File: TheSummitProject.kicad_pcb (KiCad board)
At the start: 2 copper layers, 120 x 80 mm, 81 parts, among them IC1 STM32U5F7VJT6, J1 Cortex SWD, J10 VSYS, J11 GPS PWR, J12 Sensor PWR, J13 3.3v LORA, J2 USB C, J3 Battery Connector, J4 Screen FPC, J5 Micro_SD_Card_Det1, J6 GPS, J7 LoRa, J8 Sensors, J9 RCC, Q1 NMOS, SW1 SW_SPDT, SW2 PWR_BTN, U1 NPM1300-CAAA-R, U2 USBLC6-2SC6, U3 USBLC6-2SC6, Y1 16Mhz, Y2 32.768Khz

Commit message: modify lora
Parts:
- moved J13 160.8 mm to (125.5, 106.5)
- moved D1 0.50 mm to (129.0, 104.0)
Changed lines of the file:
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@@
 	(footprint "Connector_PinHeader_2.54mm:PinHeader_1x02_P2.54mm_Vertical"
 		(layer "F.Cu")
-		(at 266.795 29.795)
+		(at 125.5 106.46)
 		(descr "Through hole straight pin header, 1x02, 2.54mm pitch, single row")
 		(tags "Through hole pin header THT 1x02 2.54mm single row")
@@
 	(footprint "LED_SMD:LED_RGB_1210"
 		(layer "F.Cu")
-		(at 128.5 104 -90)
+		(at 129 104 -90)
 		(descr "RGB LED 3.2x2.7mm http://www.avagotech.com/docs/AV02-0610EN")
 		(tags "LED 3227")

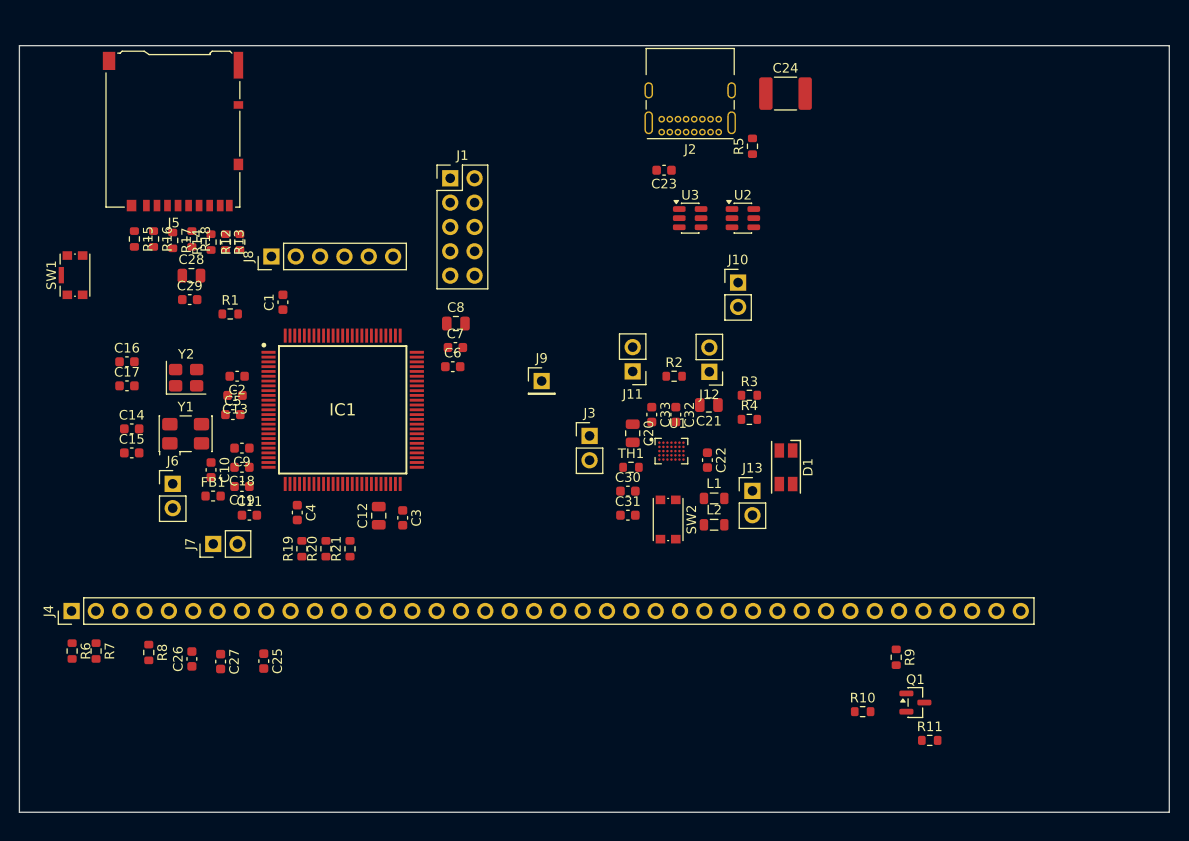
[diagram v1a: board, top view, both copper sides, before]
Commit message: wire usbc and cystal
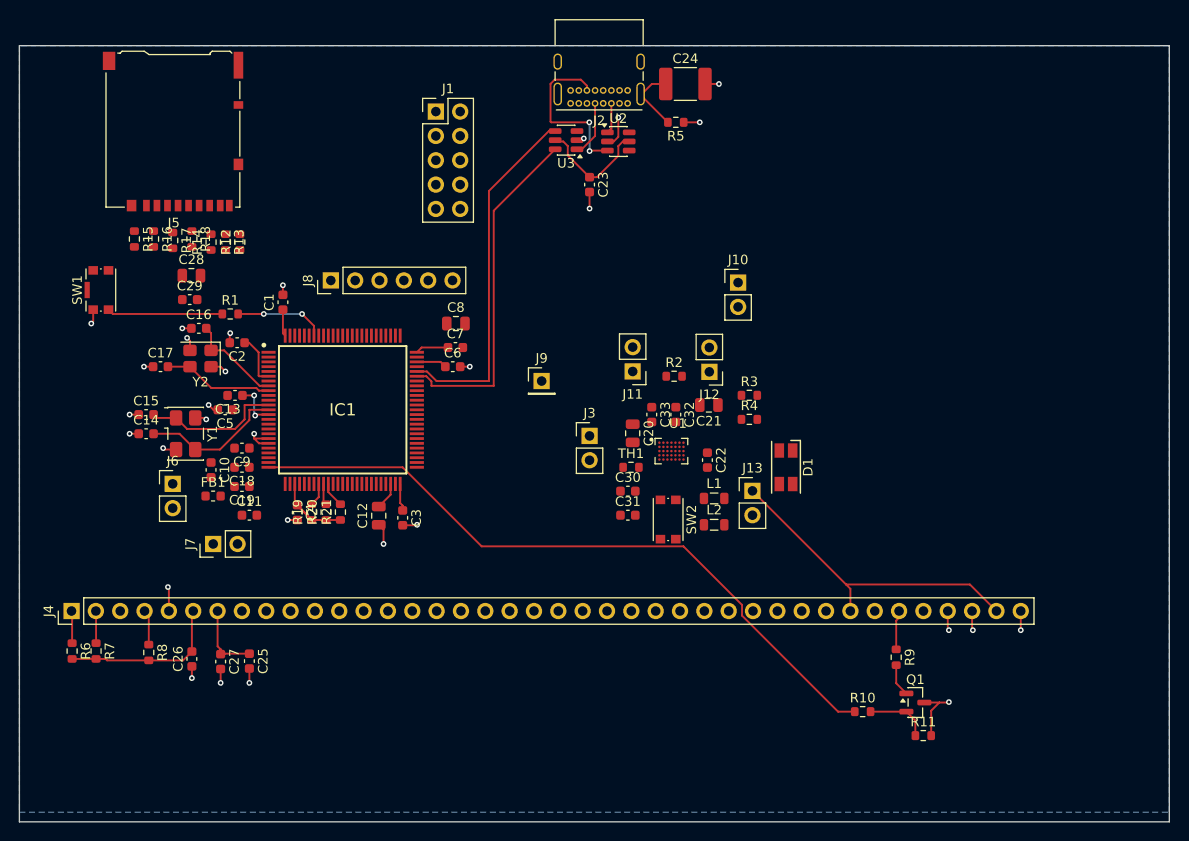
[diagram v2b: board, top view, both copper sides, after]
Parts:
- moved U3 15.3 mm to (106.0, 69.9), turned to 180 degrees
- moved U2 15.3 mm to (111.5, 70.0)
- moved C24 10.5 mm to (118.5, 64.0)
- moved J2 9.96 mm to (112.5, 66.0)
- moved R5 8.38 mm to (117.5, 68.0), turned to 180 degrees
- moved C16 8.27 mm to (67.7, 89.5)
- moved C23 7.92 mm to (108.5, 74.5), turned to -90 degrees
- moved J1 7.12 mm to (92.5, 66.9)
- moved J8 6.69 mm to (81.5, 84.5)
- moved C15 4.27 mm to (62.2, 98.5)
- moved C17 4.03 mm to (63.7, 93.5)
- moved R19 3.96 mm to (79.5, 108.7)
- moved R21 3.95 mm to (82.5, 108.7)
- moved R20 3.83 mm to (81.0, 108.7)
- moved C2 3.50 mm to (71.7, 91.0)
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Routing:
- net LCD_PWM: track 0.00 -> 72.4 mm
- net +3.3V_DP_LORA: track 0.00 -> 58.7 mm
- net GND: track 0.00 -> 51.9 mm, vias 0 -> 30
- net Net-(IC1-USB_OTG_HS_DP): track 0.00 -> 37.3 mm
- net Net-(IC1-USB_OTG_HS_DM): track 0.00 -> 36.1 mm
- net +3.3V: track 0.00 -> 29.3 mm
- net Net-(J2-CC2): track 0.00 -> 17.7 mm, vias 0 -> 2
- net Net-(IC1-HSE_OUT): track 0.00 -> 15.2 mm
- net Net-(IC1-HSE_IN): track 0.00 -> 14.5 mm
- net VBUS: track 0.00 -> 12.1 mm
- net Net-(SW1-B): track 0.00 -> 12.1 mm
- net Net-(IC1-LSE_OUT): track 0.00 -> 11.5 mm
- net Net-(IC1-LSE_IN): track 0.00 -> 10.0 mm
- net /MCU/SW_BOOT0: track 0.00 -> 9.45 mm, vias 0 -> 2
- net Net-(J2-SHIELD): track 0.00 -> 7.19 mm
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- added copper zone on B.Cu, net GND
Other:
- board size 120 x 80 mm -> 120 x 81 mm

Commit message: pcb wiring
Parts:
- moved J8 1.50 mm to (81.4, 86.0)
- turned C28 to 180 degrees
- turned C29 to 180 degrees
- turned R13 to 90 degrees
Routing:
- net +3.3V: track 29.3 -> 85.9 mm, vias 0 -> 6
- net LCD_D15: track 0.00 -> 55.1 mm, vias 0 -> 8
- net LCD_D14: track 0.00 -> 53.8 mm, vias 0 -> 6
- net LCD_D13: track 0.00 -> 50.8 mm, vias 0 -> 7
- net LCD_D12: track 0.00 -> 46.5 mm, vias 0 -> 9
- net SD_D1: track 0.00 -> 44.4 mm, vias 0 -> 2
- net SD_D0: track 0.00 -> 43.4 mm, vias 0 -> 7
- net SD_DETECT: track 0.00 -> 42.2 mm, vias 0 -> 2
- net SD_D2: track 0.00 -> 39.9 mm, vias 0 -> 6
- net SD_D3: track 0.00 -> 35.9 mm, vias 0 -> 2
- net LCD_RS: track 0.00 -> 34.9 mm, vias 0 -> 2
- net SD_CMD: track 0.00 -> 30.0 mm, vias 0 -> 5
- net SD_CK: track 0.00 -> 29.9 mm, vias 0 -> 4
- net Net-(IC1-DEBUG_JTMS-SWDIO): track 0.00 -> 29.7 mm, vias 0 -> 2
- net LCD_D1: track 0.00 -> 26.1 mm, vias 0 -> 2
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
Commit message: changed NPM1300 BGA to QFN footprint
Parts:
- added C30: 1u, Capacitor_SMD:C_0603_1608Metric, F.Cu at (157.0, 64.8)
- added C31: 1u, Capacitor_SMD:C_0603_1608Metric, F.Cu at (157.0, 67.3)
- added C32: 2.2u, Capacitor_SMD:C_0603_1608Metric, F.Cu at (157.0, 69.8)
- added C33: 2.2u, Capacitor_SMD:C_0603_1608Metric, F.Cu at (157.0, 72.3)
- added L2: 2.2u, Inductor_SMD:L_0805_2012Metric, F.Cu at (161.3, 69.5)
- added R2: 4.7k, Resistor_SMD:R_0603_1608Metric, F.Cu at (157.0, 74.8)
- added R3: 4.7k, Resistor_SMD:R_0603_1608Metric, F.Cu at (157.0, 77.3)
- added R4: 350k, Resistor_SMD:R_0603_1608Metric, F.Cu at (157.0, 79.8)
- added SW2: PWR_BTN, Button_Switch_SMD:SW_Push_1P1T_NO_CK_KMR2, F.Cu at (162.3, 65.8)
- added TH1: 10k, Resistor_SMD:R_0603_1608Metric, F.Cu at (157.0, 82.3)
- U1: footprint TheSummitProject:BGA35N44X41P5X7_237X307X51 -> TheSummitProject:QFN32_5X5_NOR

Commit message: changed screen footprint
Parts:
- J4: footprint Connector_PinHeader_2.54mm:PinHeader_1x40_P2.54mm_Vertical -> Connector_FFC-FPC:Amphenol_F32Q-1A7x1-11039_1x39-1MP_P0.5mm_Horizontal
- moved J4 40.7 mm to (94.0, 128.4), turned to 0 degrees

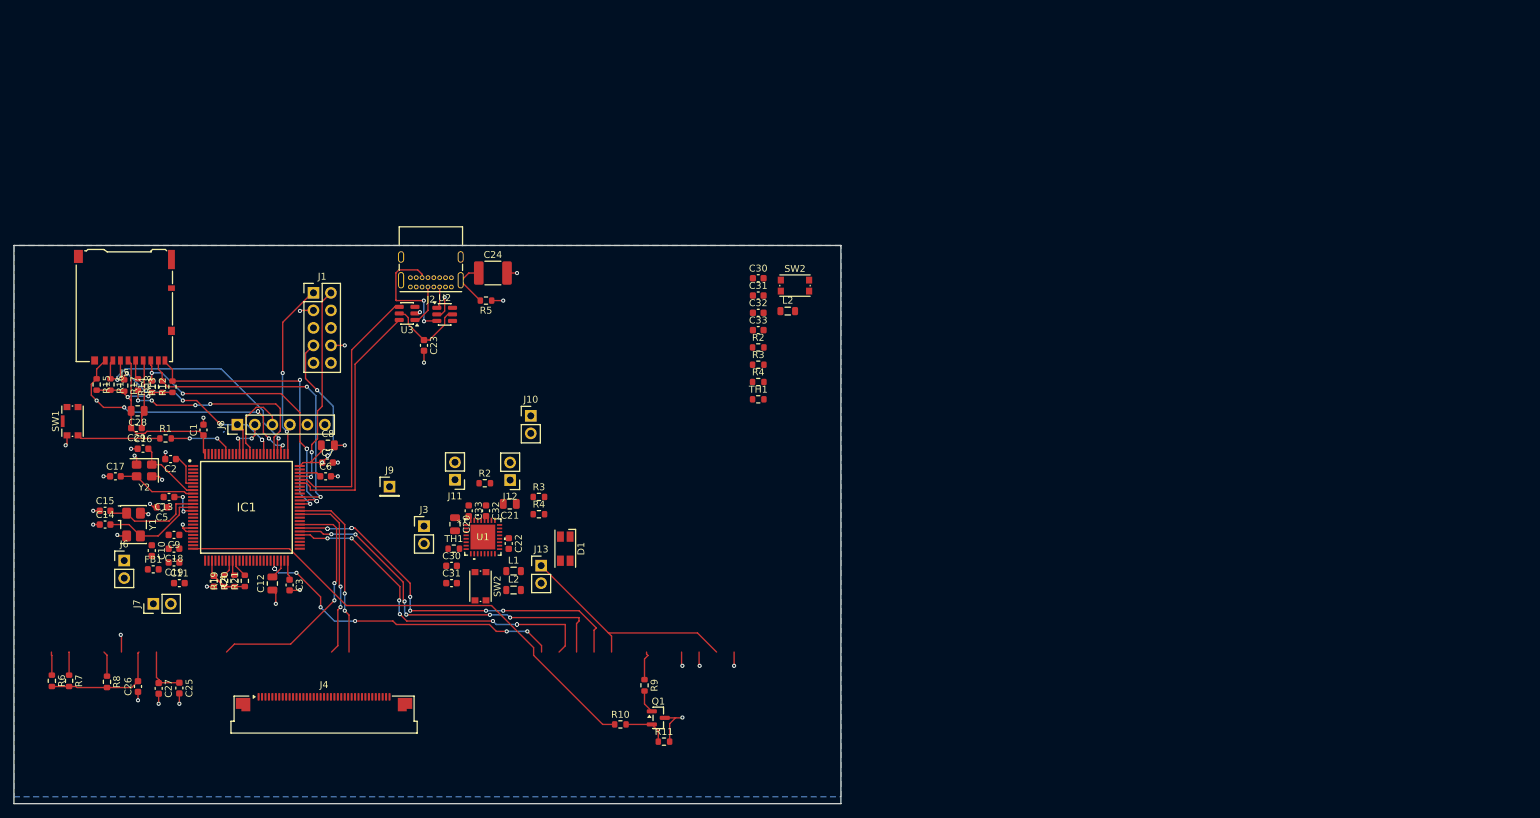
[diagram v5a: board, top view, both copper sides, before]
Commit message: Changed pcb to 4 layers and completed 50% traces
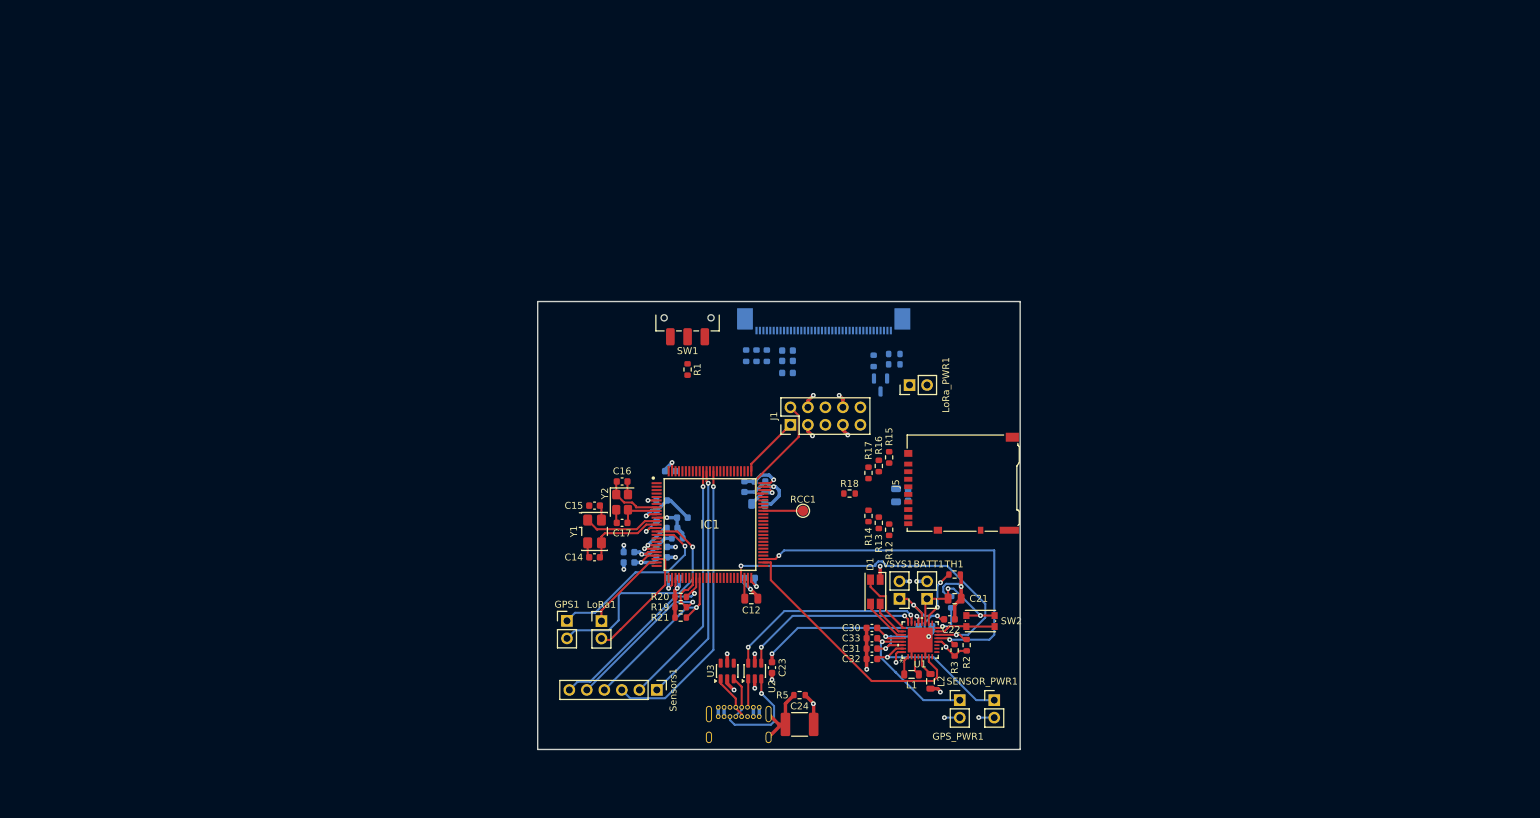
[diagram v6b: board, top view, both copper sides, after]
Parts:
- removed the C30 at (112.5, 106.5)
- removed the C30 at (157.0, 64.8)
- removed the C31 at (112.5, 109.0)
- removed the C31 at (157.0, 67.3)
- removed the C32 at (157.0, 69.8)
- removed the C32 at (117.5, 98.5)
- removed the C33 at (157.0, 72.3)
- removed the C33 at (115.0, 98.5)
- removed J10: VSYS, Connector_PinHeader_2.54mm:PinHeader_1x02_P2.54mm_Vertical
- removed J11: GPS PWR, Connector_PinHeader_2.54mm:PinHeader_1x02_P2.54mm_Vertical
- removed J12: Sensor PWR, Connector_PinHeader_2.54mm:PinHeader_1x02_P2.54mm_Vertical
- removed J13: 3.3v LORA, Connector_PinHeader_2.54mm:PinHeader_1x02_P2.54mm_Vertical
- removed J2: USB C, Connector_USB:USB_C_Receptacle_GCT_USB4085
- removed J3: Battery Connector, Connector_PinHeader_2.54mm:PinHeader_1x02_P2.54mm_Vertical
- removed J6: GPS, Connector_PinHeader_2.54mm:PinHeader_1x02_P2.54mm_Vertical
- removed J7: LoRa, Connector_PinHeader_2.54mm:PinHeader_1x02_P2.54mm_Vertical
- removed J8: Sensors, Connector_PinHeader_2.54mm:PinHeader_1x06_P2.54mm_Vertical
- removed J9: RCC, Connector_PinHeader_2.54mm:PinHeader_1x01_P2.54mm_Vertical
- removed the L2 at (161.3, 69.5)
- removed the L2 at (121.5, 110.0)
- removed the R2 at (117.3, 94.5)
- removed the R2 at (157.0, 74.8)
- removed the R3 at (125.2, 96.5)
- removed the R3 at (157.0, 77.3)
- removed the R4 at (157.0, 79.8)
- removed the R4 at (125.2, 99.0)
- removed the SW2 at (116.7, 109.5)
- removed the SW2 at (162.3, 65.8)
- removed the TH1 at (157.0, 82.3)
- removed the TH1 at (112.8, 104.0)
- added BATT1: Battery Connector, Connector_PinHeader_2.54mm:PinHeader_1x02_P2.54mm_Vertical, F.Cu at (181.5, 111.3)
- added C30: 1u, Capacitor_SMD:C_0603_1608Metric, F.Cu at (173.5, 115.5)
- added C31: 1u, Capacitor_SMD:C_0603_1608Metric, F.Cu at (173.5, 118.5)
- added C32: 2.2u, Capacitor_SMD:C_0603_1608Metric, F.Cu at (173.5, 120.0)
- added C33: 2.2u, Capacitor_SMD:C_0603_1608Metric, F.Cu at (173.5, 117.0)
- added GPS1: GPS, Connector_PinHeader_2.54mm:PinHeader_1x02_P2.54mm_Vertical, F.Cu at (129.2, 114.5)
- added GPS_PWR1: GPS PWR, Connector_PinHeader_2.54mm:PinHeader_1x02_P2.54mm_Vertical, F.Cu at (186.2, 126.0)
- added L2: 2.2u, Inductor_SMD:L_0805_2012Metric, F.Cu at (182.0, 123.2)
- added LoRa1: LoRa, Connector_PinHeader_2.54mm:PinHeader_1x02_P2.54mm_Vertical, F.Cu at (134.2, 114.5)
- added LoRa_PWR1: 3.3v LORA, Connector_PinHeader_2.54mm:PinHeader_1x02_P2.54mm_Vertical, F.Cu at (179.0, 80.2)
- added R2: 4.7k, Resistor_SMD:R_0603_1608Metric, F.Cu at (187.2, 118.0)
- added R3: 4.7k, Resistor_SMD:R_0603_1608Metric, F.Cu at (185.5, 118.8)
- added R4: 350k, Resistor_SMD:R_0603_1608Metric, B.Cu at (185.0, 111.8)
- added RCC1: RCC, TestPoint:TestPoint_Pad_D1.5mm, F.Cu at (163.5, 98.5)
- added SENSOR_PWR1: Sensor PWR, Connector_PinHeader_2.54mm:PinHeader_1x02_P2.54mm_Vertical, F.Cu at (191.2, 126.0)
- added SW2: PWR_BTN, Button_Switch_SMD:SW_Push_1P1T_NO_CK_KMR2, F.Cu at (189.2, 114.5)
- added Sensors1: Sensors, Connector_PinHeader_2.54mm:PinHeader_1x06_P2.54mm_Vertical, F.Cu at (142.3, 124.5)
- added TH1: 10k, Resistor_SMD:R_0603_1608Metric, F.Cu at (185.5, 107.8)
- added USB-C1: USB C, Connector_USB:USB_C_Receptacle_GCT_USB4085, B.Cu at (157.2, 127.0)
- added VSYS1: VSYS, Connector_PinHeader_2.54mm:PinHeader_1x02_P2.54mm_Vertical, F.Cu at (177.5, 111.3)
- C1, C10, C11, C13, C18, C19, C2, C20, C25, C26, C27, C28, C29, C3, C4, C5, C6, C7, C8, C9, FB1, Q1, R10, R11, R6, R7, R8, R9: moved to B.Cu
- J4: footprint Connector_FFC-FPC:Amphenol_F32Q-1A7x1-11039_1x39-1MP_P0.5mm_Horizontal -> Connector_FFC-FPC:TE_4-1734839-0_1x40-1MP_P0.5mm_Horizontal; moved to B.Cu
- SW1: footprint Button_Switch_SMD:SW_Push_1P1T-SH_NO_CK_KMR2xxG -> Button_Switch_SMD:SW_SPDT_CK_JS102011SAQN
- moved J5 124.1 mm to (186.5, 94.5), turned to 90 degrees
- moved R15 115.5 mm to (176.0, 90.8), turned to 90 degrees
- moved C29 112.4 mm to (178.8, 96.2), turned to 90 degrees
- moved R16 112.1 mm to (174.5, 92.0), turned to 90 degrees
- moved R6 111.2 mm to (155.2, 76.0)
- moved C28 110.7 mm to (177.0, 96.2), turned to 90 degrees
- moved R7 110.3 mm to (156.8, 76.0)
- moved R17 108.7 mm to (173.0, 93.0), turned to 90 degrees
- moved R8 106.8 mm to (158.2, 76.0)
- moved C26 106.1 mm to (161.2, 75.2), turned to 180 degrees
- moved R12 106.0 mm to (176.0, 101.2)
- moved R13 105.9 mm to (174.5, 100.2)
- moved R14 105.7 mm to (173.0, 99.2)
- moved R18 104.5 mm to (170.2, 96.0), turned to 0 degrees
- moved C27 102.1 mm to (161.2, 78.5), turned to 0 degrees
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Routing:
- net LCD_PWM: track 72.4 -> 0.00 mm
- net PM_SDA: track 0.00 -> 56.0 mm, vias 0 -> 2
- net +3.3V_DP_LORA: track 58.7 -> 2.81 mm
- net LCD_D15: track 55.1 -> 0.00 mm, vias 8 -> 0
- net LCD_D14: track 53.8 -> 0.00 mm, vias 6 -> 0
- net PM_SCL: track 0.00 -> 52.2 mm, vias 0 -> 2
- net LCD_D13: track 50.8 -> 0.00 mm, vias 7 -> 0
- net LCD_D12: track 46.5 -> 0.00 mm, vias 9 -> 0
- net GND: track 68.1 -> 114.6 mm, vias 34 -> 24
- net SD_D1: track 44.4 -> 0.00 mm, vias 2 -> 0
- net SD_D0: track 43.4 -> 0.00 mm, vias 7 -> 0
- net SD_DETECT: track 42.2 -> 0.00 mm, vias 2 -> 0
- net +3.3V: track 85.9 -> 45.6 mm, vias 6 -> 12
- net SD_D2: track 39.9 -> 0.00 mm, vias 6 -> 0
- net NPM_INT: track 0.00 -> 37.5 mm
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- added copper zone on In2.Cu, net +3.3V
- added copper zone on In2.Cu, net +3.3V_DP_LORA
- added copper zone on In1.Cu, net GND
- added copper zone on In2.Cu, net VBUS
- removed copper zone on B.Cu, net GND
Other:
- board size 120 x 81 mm -> 70 x 65 mm
- copper layers 2 -> 4
